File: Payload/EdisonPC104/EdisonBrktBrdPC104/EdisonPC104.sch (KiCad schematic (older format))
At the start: 10 parts, among them J17 CONN_14, J18 CONN_14, J19 CONN_14, J20 CONN_14, K1 CONN_3, K2 CONN_3, U1 ADG3308, U2 ADG3308

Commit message: se agrega piezas pequeñas de lanzador de langmuir probe
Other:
- note added: "VSYS acepta rangos 3.15V-4.5V. \nCuando se usa la BrktBrd VSYS se alimenta a traves \ndel Ored de 5V_USB con VIN (7V-15V) -obviamente \ncon reguladores de por medio-.\nEn esta placa se conectó VCC del PC104 a VSYS (3.3V)\npara energizar al Edison"
- note removed: "VSYS acepta rangos 3.15V-4.5V. \nCuando se usa la BrktBrd VSYS se alimenta a traves \ndel Ored de 5V_USB con VIN (7V-15V) -obviamente \ncon reguladores de por medio-.\nEn esta placa conecta VCC del PC104 a VSYS (3.3V)\npara energizar al Edison"
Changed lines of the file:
@@
 $EndComp
 Text Notes 7250 5800 0    60   ~ 0
-VSYS acepta rangos 3.15V-4.5V. \nCuando se usa la BrktBrd VSYS se alimenta a traves \ndel Ored de 5V_USB con VIN (7V-15V) -obviamente \ncon reguladores de por medio-.\nEn esta placa conecta VCC del PC104 a VSYS (3.3V)\npara energizar al Edison
+VSYS acepta rangos 3.15V-4.5V. \nCuando se usa la BrktBrd VSYS se alimenta a traves \ndel Ored de 5V_USB con VIN (7V-15V) -obviamente \ncon reguladores de por medio-.\nEn esta placa se conectó VCC del PC104 a VSYS (3.3V)\npara energizar al Edison
 Text Notes 950  7650 0    60   ~ 0
 UART2 del Edison es por \ndefecto el serial port \ndebug de Linux. UART2 \nseria tambien el UART \nque va al FTDI en la BrkBrd

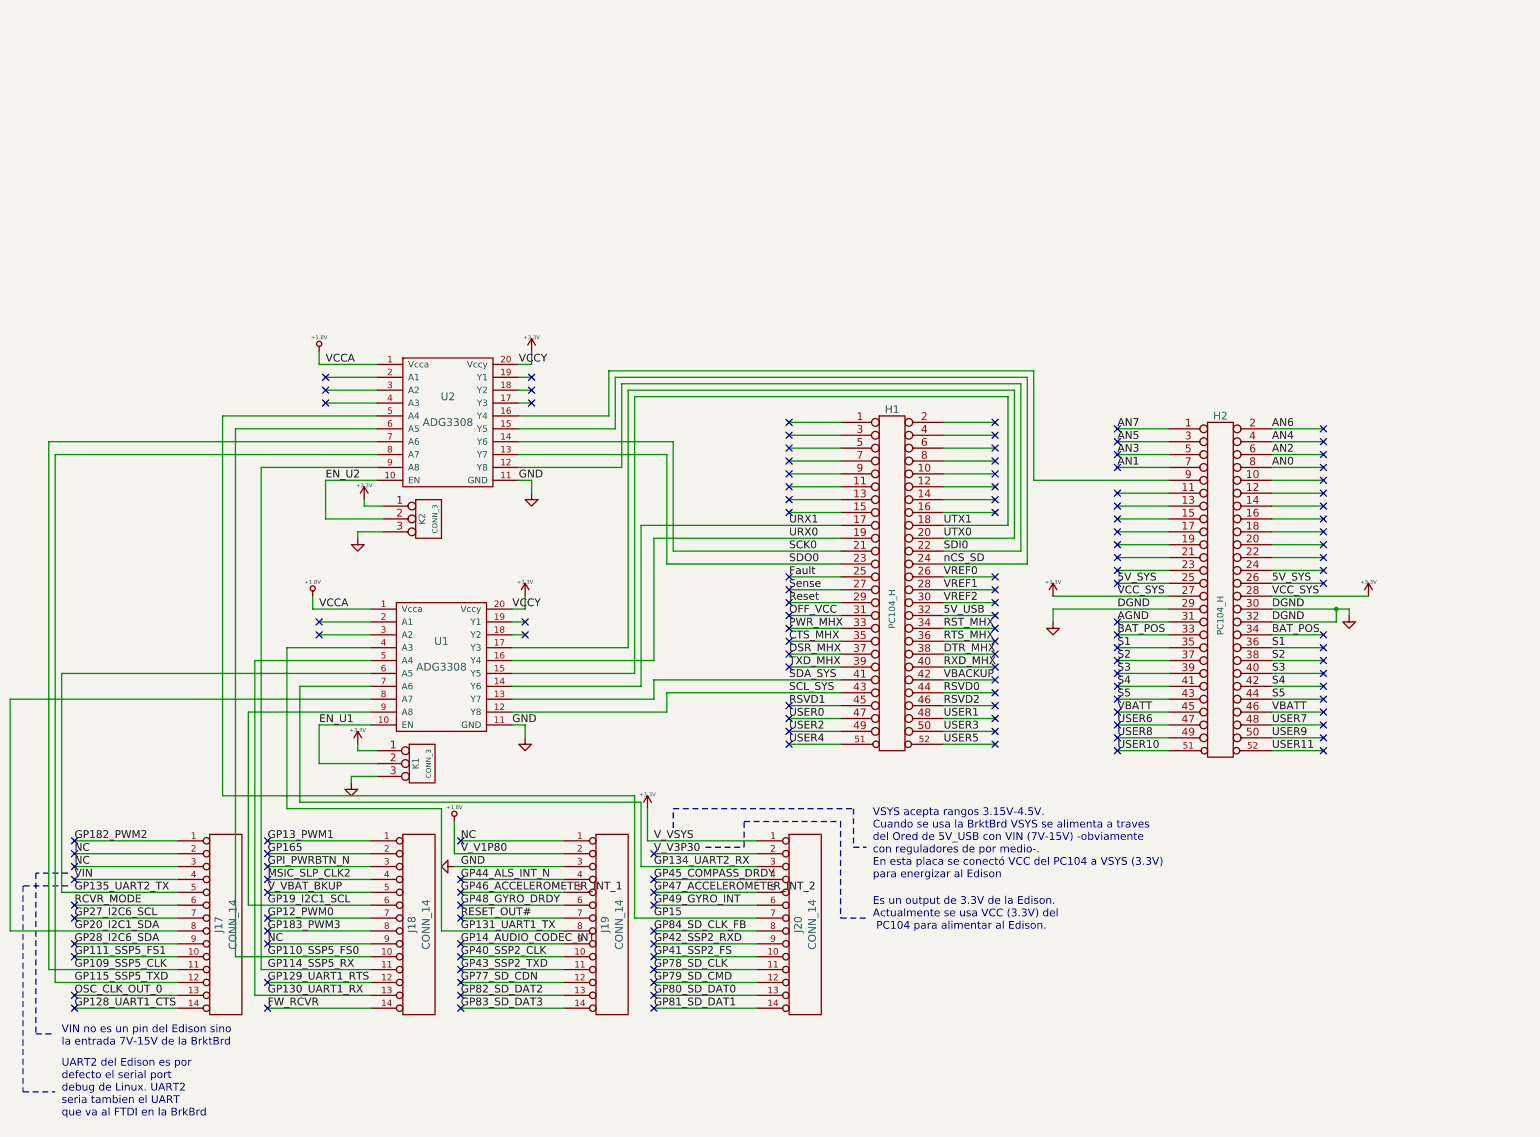
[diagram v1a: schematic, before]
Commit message: se crea nueva version de placa para alojar Rasp Zero y Edison. Se parte con arreglar los errores detectados en la parte de Edison
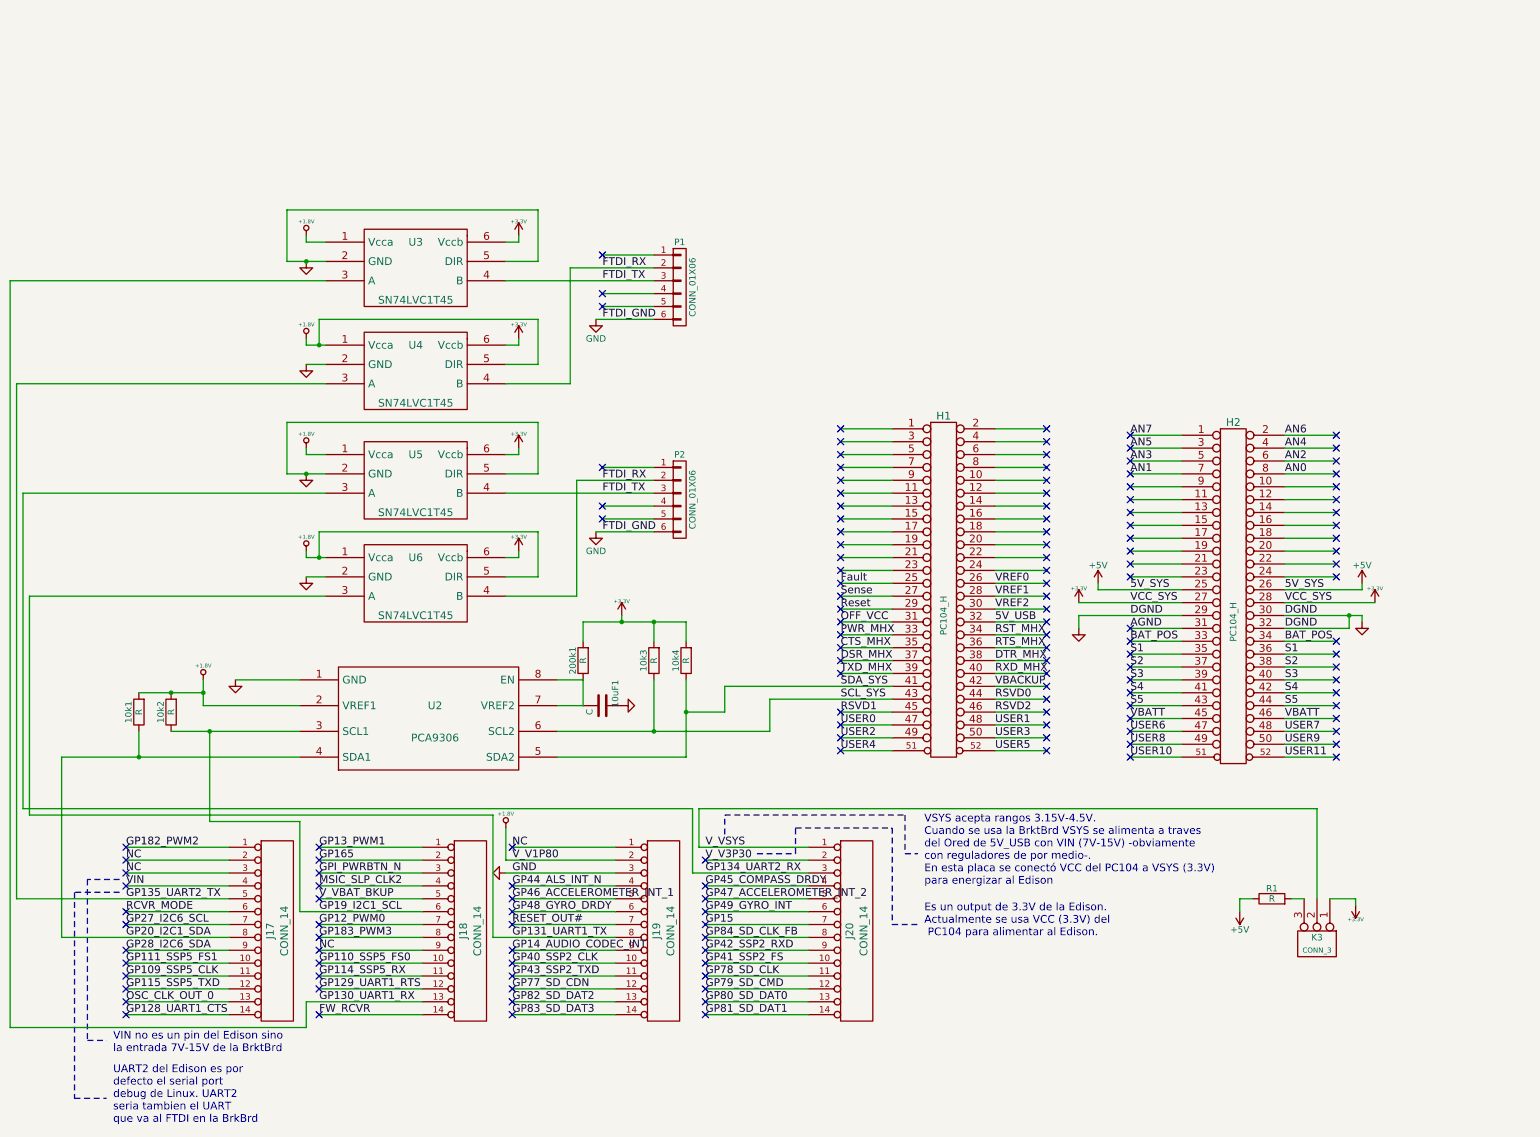
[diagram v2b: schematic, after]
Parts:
- removed K1, K2: CONN_3, Pin_Headers:Pin_Header_Straight_1x03, symbol CONN_3
- removed U1, U2: ADG3308, Housings_SSOP:TSSOP-20_4.4x6.5mm_Pitch0.65mm, symbol ADG3308
- added 10k1, 10k2, 10k3, 10k4, 200k1: R, Resistors_SMD:R_1206_HandSoldering, symbol R
- added 10uF1: C, SMD_Packages:SMD-1206_Pol, symbol C
- added K3: CONN_3, Pin_Headers:Pin_Header_Straight_1x03, symbol CONN_3
- added P1, P2: CONN_01X06, Pin_Headers:Pin_Header_Angled_1x06, symbol CONN_01X06
- added R1: R, Resistors_ThroughHole:Resistor_Horizontal_RM15mm, symbol R
- added U2: PCA9306, SMD_Packages:SOIC-8-N, symbol PCA9306
- added U3, U4, U5, U6: SN74LVC1T45, TO_SOT_Packages_SMD:SOT-23-6, symbol SN74LVC1T45
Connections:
- net +1.8V: now also 10k1.2, 10k2.2, U2.2 (VREF1), U3.1 (Vcca), U4.1 (Vcca), U4.5 (DIR), U5.1 (Vcca), U6.1 (Vcca), U6.5 (DIR)
- net +3V3: now also 10k3.2, 10k4.2, 200k1.2, K3.1 (P1), U3.6 (Vccb), U4.6 (Vccb), U5.6 (Vccb), U6.6 (Vccb); no longer J20.1 (P1)
- net GND: now also 10uF1.1, P1.6 (P6), P2.6 (P6), U2.1 (GND), U3.2 (GND), U3.5 (DIR), U4.2 (GND), U5.2 (GND), U5.5 (DIR), U6.2 (GND)
- net GP130_UART1_RX: now also U3.3 (A)
- net GP131_UART1_TX: now also U6.3 (A)
- net GP134_UART2_RX: now also U5.3 (A)
- net GP135_UART2_TX: now also U4.3 (A)
- net GP19_I2C1_SCL: now also 10k2.1, U2.3 (SCL1)
- net GP20_I2C1_SDA: now also 10k1.1, U2.4 (SDA1)
- net SCL_SYS: now also 10k3.1, U2.6 (SCL2)
- net SDA_SYS: now also 10k4.1, U2.5 (SDA2)
- net 5V_SYS renamed +5V
- net +5V: now also R1.1
- net SCK0: no longer names the net of H1.21 (P21)
- net SDI0: no longer names the net of H1.22 (P22)
- net SDO0: no longer names the net of H1.23 (P23)
- net URX0: no longer names the net of H1.19 (P19)
- net URX1: no longer names the net of H1.17 (P17)
- net UTX0: no longer names the net of H1.20 (P20)
- net UTX1: no longer names the net of H1.18 (P18)
- net nCS_SD: no longer names the net of H1.24 (P24)
- new net: K3.3 (P3), R1.2
- new net: 10uF1.2, 200k1.1, U2.7 (VREF2), U2.8 (EN)
- new net FTDI_RX: P1.2 (P2), P2.2 (P2), U4.4 (B), U6.4 (B)
- new net FTDI_TX: P1.3 (P3), P2.3 (P3), U3.4 (B), U5.4 (B)
- new net V_VSYS: J20.1 (P1), K3.2 (PM)
- no-connect marks 140 -> 148
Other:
- moved on the sheet: H1, H2, J17, J18, J19, J20

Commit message: se corrige bug de ruteo de UART1 y 2
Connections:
- net GP131_UART1_TX: now also U4.3 (A); no longer U6.3 (A)
- net GP135_UART2_TX: now also U6.3 (A); no longer U4.3 (A)
- net FTDI_RX renamed FTDI1_RX
- net FTDI1_RX: no longer P2.2 (P2), U6.4 (B)
- net FTDI_TX renamed FTDI1_TX
- net FTDI1_TX: no longer P2.3 (P3), U5.4 (B)
- new net FTDI2_RX: P2.2 (P2), U6.4 (B)
- new net FTDI2_TX: P2.3 (P3), U5.4 (B)
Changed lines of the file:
@@
 	2250 5850 1450 5850
 Wire Wire Line
-	700  5300 4300 5300
+	600  5300 4300 5300
 Wire Wire Line
 	4300 5300 4300 6250
@@
 Wire Wire Line
 	1450 6050 2250 6050
-Wire Wire Line
-	600  5950 2250 5950
 Wire Wire Line
 	1450 5750 2250 5750
@@
 	3000 3600 700  3600
 Wire Wire Line
-	700  3600 700  5300
-Wire Wire Line
-	650  5250 650  2800
-Wire Wire Line
 	650  2800 3000 2800
-Wire Wire Line
-	600  5950 600  1950
 Wire Wire Line
 	600  1950 3000 1950
@@
 	5100 3100 5550 3100
 Text Label 5150 3100 0    60   ~ 0
-FTDI_GND
+FTDI2_GND
 Text Label 5150 2700 0    60   ~ 0
-FTDI_RX
+FTDI2_RX
 Text Label 5150 2800 0    60   ~ 0
-FTDI_TX
+FTDI2_TX
 NoConn ~ 5150 2900
 NoConn ~ 5150 3000
@@
 	5100 1450 5550 1450
 Text Label 5150 1450 0    60   ~ 0
-FTDI_GND
+FTDI1_GND
 Text Label 5150 1050 0    60   ~ 0
-FTDI_RX
+FTDI1_RX
 Text Label 5150 1150 0    60   ~ 0
-FTDI_TX
+FTDI1_TX
 NoConn ~ 5150 1250
 NoConn ~ 5150 1350
@@
 Wire Wire Line
 	10700 5250 10700 5950
+Wire Wire Line
+	600  5300 600  1950
+Wire Wire Line
+	650  5250 650  2800
+Wire Wire Line
+	700  5950 2250 5950
+Wire Wire Line
+	700  3600 700  5950
 $EndSCHEMATC

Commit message: se declara lista la mita Edison de la placa
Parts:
- added P?: CONN_02X20, symbol CONN_02X20
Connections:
- wire segments 266 -> 318
- no-connect marks 148 -> 156
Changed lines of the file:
@@
 Wire Wire Line
 	700  3600 700  5950
+Wire Wire Line
+	8950 1000 8950 600
+Wire Wire Line
+	9050 1000 9050 600
+Wire Wire Line
+	9150 550  9150 1000
+Wire Wire Line
+	9250 1000 9250 600
+Wire Wire Line
+	9350 1000 9350 600
+Wire Wire Line
+	9450 1000 9450 600
+Wire Wire Line
+	9550 1000 9550 600
+Wire Wire Line
+	9650 550  9650 1000
+Wire Wire Line
+	9750 1000 9750 600
+Wire Wire Line
+	9850 550  9850 1000
+Wire Wire Line
+	9950 1000 9950 600
+Wire Wire Line
+	10050 1000 10050 600
+Wire Wire Line
+	10150 1000 10150 600
+Wire Wire Line
+	8950 1900 8950 1500
+Wire Wire Line
+	9050 1500 9050 1950
+Wire Wire Line
+	9150 1900 9150 1500
+Wire Wire Line
+	9250 1900 9250 1500
+Wire Wire Line
+	9350 1900 9350 1500
+Wire Wire Line
+	9450 1500 9450 2000
+Wire Wire Line
+	9550 1900 9550 1500
+Wire Wire Line
+	9650 1900 9650 1500
+Wire Wire Line
+	9750 1900 9750 1500
+Wire Wire Line
+	9850 1900 9850 1500
+Wire Wire Line
+	9950 1900 9950 1500
+Wire Wire Line
+	10050 1900 10050 1500
+Wire Wire Line
+	10150 2000 10150 1500
+$Comp
+L CONN_02X20 P?
+U 1 1 57080859
+P 9200 1250
+F 0 "P?" H 9200 2300 50  0000 C CNN
+F 1 "CONN_02X20" V 9200 1250 50  0000 C CNN
+F 2 "" H 9200 300 60  0000 C CNN
+F 3 "" H 9200 300 60  0000 C CNN
+	1    9200 1250
+	0    -1   -1   0
+$EndComp
+Wire Wire Line
+	8350 600  8350 1000
+Wire Wire Line
+	8450 550  8450 1000
+Wire Wire Line
+	8550 1000 8550 600
+Wire Wire Line
+	8650 1000 8650 600
+Wire Wire Line
+	8750 1000 8750 600
+Wire Wire Line
+	8850 550  8850 1000
+Wire Wire Line
+	8250 1000 8250 600
+Wire Wire Line
+	8250 1500 8250 1950
+Wire Wire Line
+	8350 1900 8350 1500
+Wire Wire Line
+	8450 1900 8450 1500
+Wire Wire Line
+	8550 1900 8550 1500
+Wire Wire Line
+	8650 1500 8650 2000
+Wire Wire Line
+	8750 1900 8750 1500
+Wire Wire Line
+	8850 1900 8850 1500
+NoConn ~ 10150 600
+NoConn ~ 10050 600
+NoConn ~ 9950 600
+NoConn ~ 10050 1900
+NoConn ~ 9950 1900
+NoConn ~ 9850 1900
+NoConn ~ 9750 1900
+NoConn ~ 9650 1900
+$Comp
+L GND #PWR?
+U 1 1 570812B4
+P 7500 1350
+F 0 "#PWR?" H 7500 1350 30  0001 C CNN
+F 1 "GND" H 7500 1280 30  0001 C CNN
+F 2 "" H 7500 1350 60  0000 C CNN
+F 3 "" H 7500 1350 60  0000 C CNN
+	1    7500 1350
+	1    0    0    -1
+$EndComp
+$Comp
+L +3.3V #PWR?
+U 1 1 570812BA
+P 7400 1000
+F 0 "#PWR?" H 7400 960 30  0001 C CNN
+F 1 "+3.3V" H 7400 1110 30  0000 C CNN
+F 2 "" H 7400 1000 60  0000 C CNN
+F 3 "" H 7400 1000 60  0000 C CNN
+	1    7400 1000
+	1    0    0    -1
+$EndComp
+$Comp
+L +5V #PWR?
+U 1 1 570812C0
+P 7650 1000
+F 0 "#PWR?" H 7650 850 50  0001 C CNN
+F 1 "+5V" H 7650 1140 50  0000 C CNN
+F 2 "" H 7650 1000 60  0000 C CNN
+F 3 "" H 7650 1000 60  0000 C CNN
+	1    7650 1000
+	1    0    0    -1
+$EndComp
+Wire Wire Line
+	7500 550  7500 1350
+Wire Wire Line
+	7650 1050 7650 1000
+Wire Wire Line
+	7400 1000 7400 1900
+Wire Wire Line
+	8150 600  8350 600
+Wire Wire Line
+	8150 600  8150 1050
+Wire Wire Line
+	8150 1050 7650 1050
+Connection ~ 8250 600
+Wire Wire Line
+	7400 1900 8250 1900
+Wire Wire Line
+	7500 550  9850 550
+Wire Wire Line
+	7650 2000 10150 2000
+Wire Wire Line
+	7650 2000 7650 1200
+Wire Wire Line
+	7650 1200 7500 1200
+Connection ~ 7500 1200
+Connection ~ 8450 550
+Connection ~ 8850 550
+Connection ~ 9150 550
+Connection ~ 9650 550
+Connection ~ 8650 2000
+Connection ~ 9450 2000
+Wire Wire Line
+	8250 1950 9050 1950
+Connection ~ 8250 1900
 $EndSCHEMATC
